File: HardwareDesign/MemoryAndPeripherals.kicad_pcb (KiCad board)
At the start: 2 copper layers, 150 x 90 mm, 29 parts, among them J001 Conn_02x40_Odd_Even, J303 Conn_01x05, J304 Conn_01x05, J305 Conn_01x09, J306 Conn_01x09, U200 28C256, U201 HM62256BLP-7SL, U301 82C55A, U302 82C54, U303 MC6850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

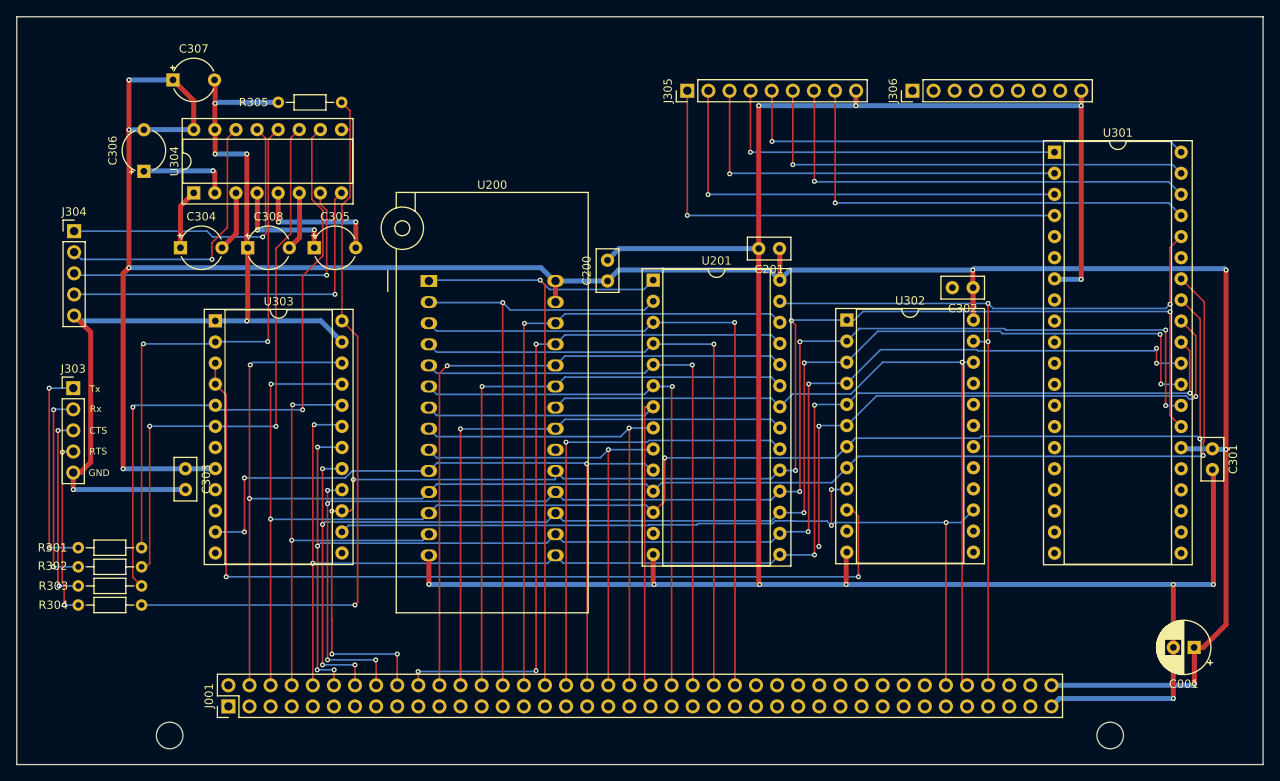
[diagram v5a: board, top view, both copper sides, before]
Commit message: all non-GND signals routed
Removed all explicit traces/vias for GND, since there
will be a ground plane on both layers.
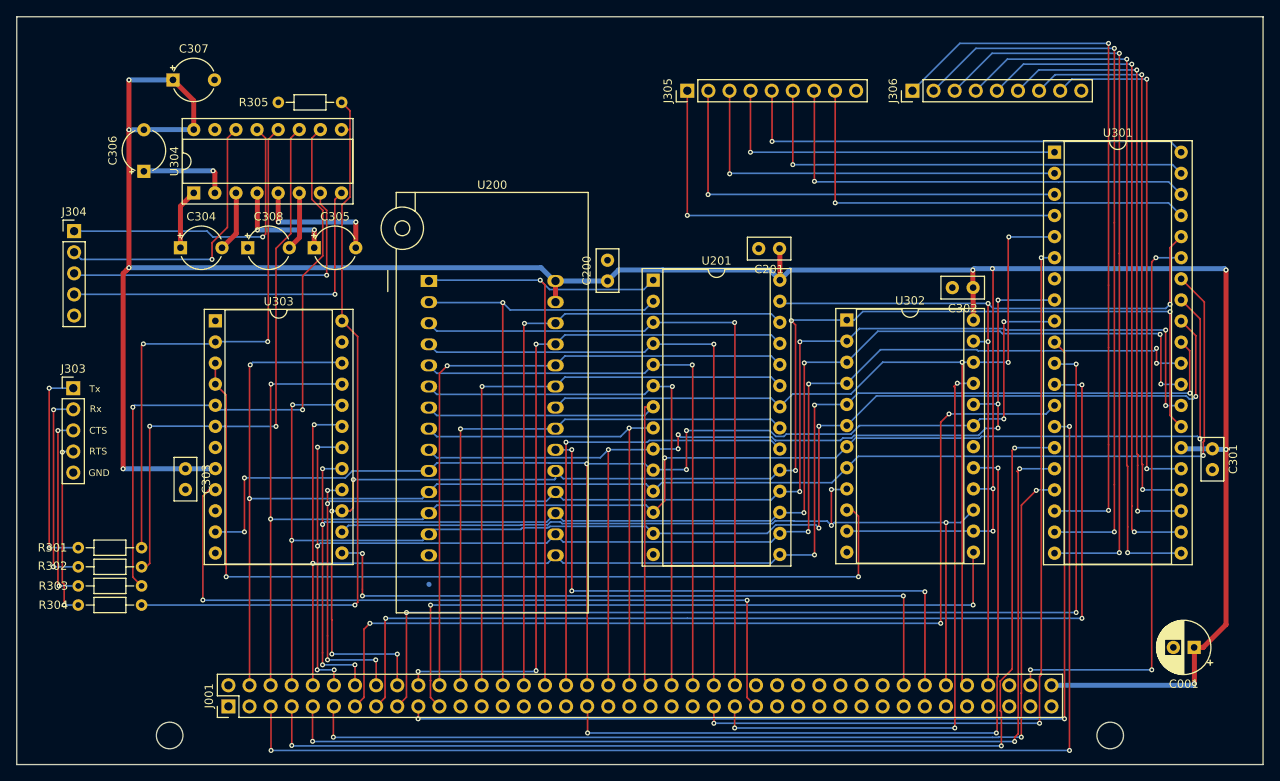
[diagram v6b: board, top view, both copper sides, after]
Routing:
- net GND: track 402.0 -> 0.76 mm, vias 16 -> 0
- net /PC0: track 0.00 -> 142.4 mm, vias 0 -> 3
- net /PC1: track 0.00 -> 131.6 mm, vias 0 -> 3
- net /PC5: track 0.00 -> 126.3 mm, vias 0 -> 3
- net /PC2: track 0.00 -> 126.1 mm, vias 0 -> 3
- net /PC7: track 0.00 -> 125.1 mm, vias 0 -> 2
- net /PC6: track 0.00 -> 124.9 mm, vias 0 -> 3
- net /PC3: track 0.00 -> 119.2 mm, vias 0 -> 3
- net /PC4: track 0.00 -> 118.2 mm, vias 0 -> 3
- net /~IODEV0: track 0.00 -> 98.9 mm, vias 0 -> 3
- net /~IODEV2: track 0.00 -> 93.1 mm, vias 0 -> 2
- net /CorePeriphs/PB2: track 0.00 -> 89.6 mm, vias 0 -> 2
- net /CorePeriphs/PB1: track 0.00 -> 89.3 mm, vias 0 -> 2
- net /CorePeriphs/PB0: track 0.00 -> 88.7 mm, vias 0 -> 2
- net /TCOUNT2: track 0.00 -> 87.4 mm, vias 0 -> 3
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
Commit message: put all desired designators on front silkscreen
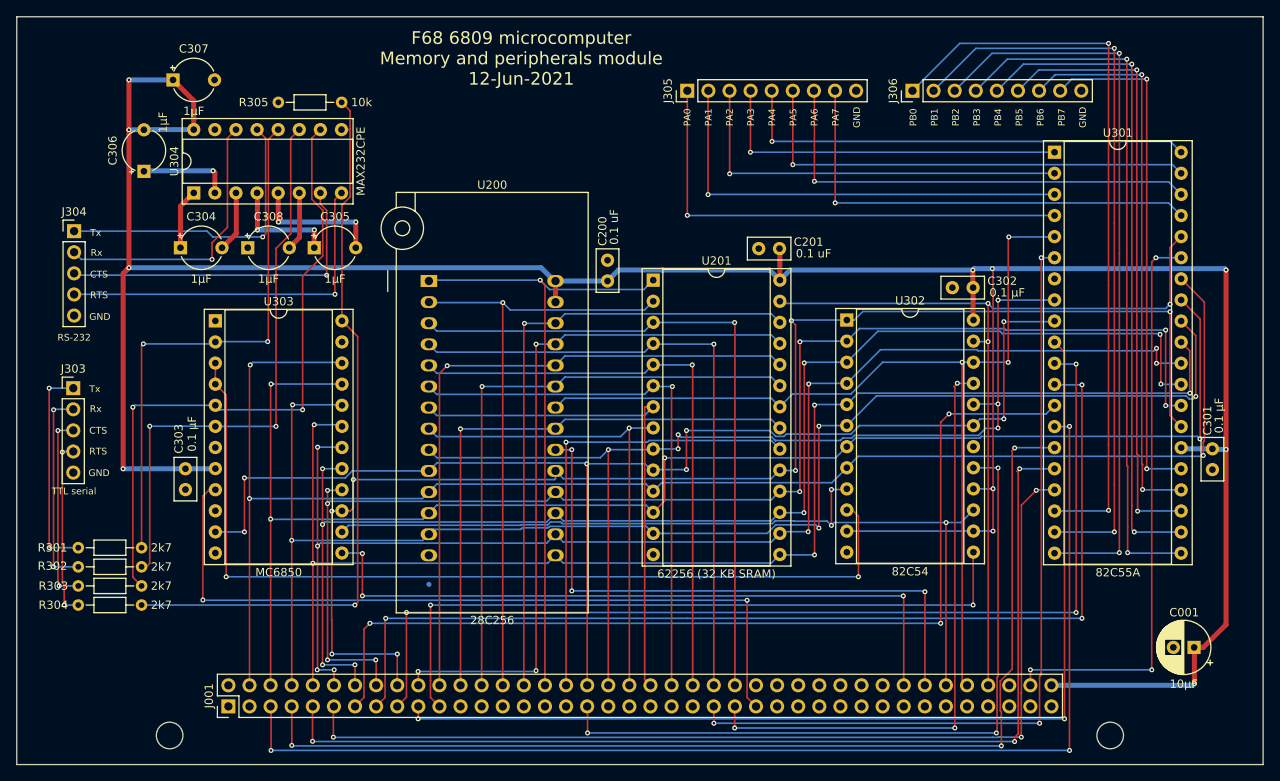
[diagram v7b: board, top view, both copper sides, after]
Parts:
- U201: value HM62256BLP-7SL -> 62256 (32 KB SRAM)
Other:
- board text added: "F68 6809 microcomputer Memory and peripherals module 12-Jun-2021"
- board text added: "PA0"
- board text added: "PA1"
- board text added: "PA2"
- board text added: "PA3"
- board text added: "PA4"
- board text added: "PA5"
- board text added: "PA6"
- board text added: "PA7"
- board text added: "PB0"
- board text added: "PB1"
- board text added: "PB2"
- board text added: "PB3"
- board text added: "PB4"
- board text added: "PB5"
- board text added: "PB6"
- board text added: "PB7"
- board text added: "RS-232"
- board text added: "TTL serial"

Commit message: add ground planes
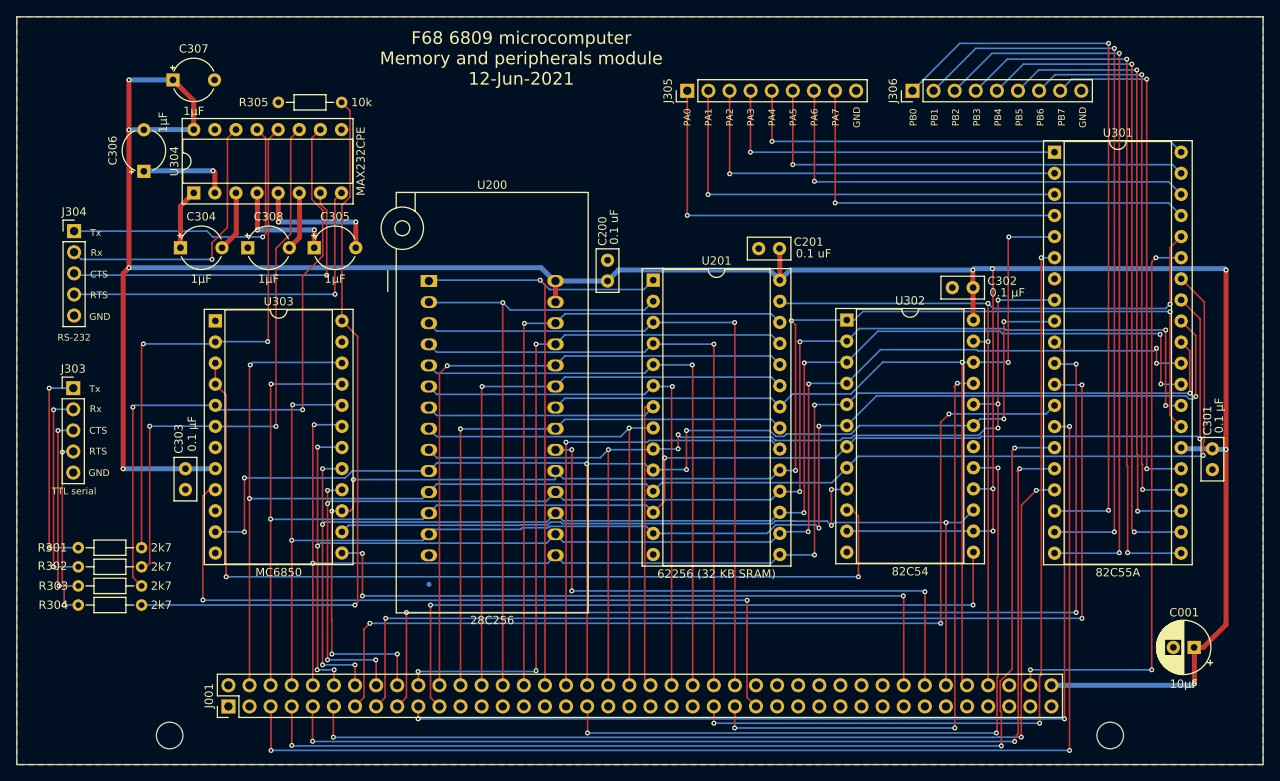
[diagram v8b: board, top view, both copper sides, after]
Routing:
- added copper zone on B.Cu, net GND
- added copper zone on F.Cu, net GND
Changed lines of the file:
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@@
   (segment (start 25.2 67.4) (end 25.2 45.52) (width 0.2) (layer Front) (net 115))
   (segment (start 23.9 41.68) (end 23.9 44.22) (width 0.2) (layer Front) (net 115))
+  (zone (net 2) (net_name GND) (layer Front) (hatch edge 0.508)
+    (connect_pads (clearance 0.508))
+    (min_thickness 0.254)
+    (fill yes (arc_segments 32) (thermal_gap 0.508) (thermal_bridge_width 0.508))
+    (polygon
+      (pts
+        (xy 150 90) (xy 0 90) (xy 0 0) (xy 150 0)
+      )
+    )
+  )
+  (zone (net 2) (net_name GND) (layer Back) (hatch edge 0.508)
+    (connect_pads (clearance 0.508))
+    (min_thickness 0.254)
+    (fill yes (arc_segments 32) (thermal_gap 0.508) (thermal_bridge_width 0.508))
+    (polygon
+      (pts
+        (xy 150 90) (xy 0 90) (xy 0 0) (xy 150 0)
+      )
+    )
+  )
 )
